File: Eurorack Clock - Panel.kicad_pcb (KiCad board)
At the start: 2 copper layers, 30 x 128.5 mm, 18 parts, among them J10X CLK/16, J3X Clock In, J6X CLK, J7X CLK/2, J8X CLK/4, J9X CLK/8, SW1X RotaryEncoder_DualWithSwitch, SW2X Run/Stop, SW3X Reset

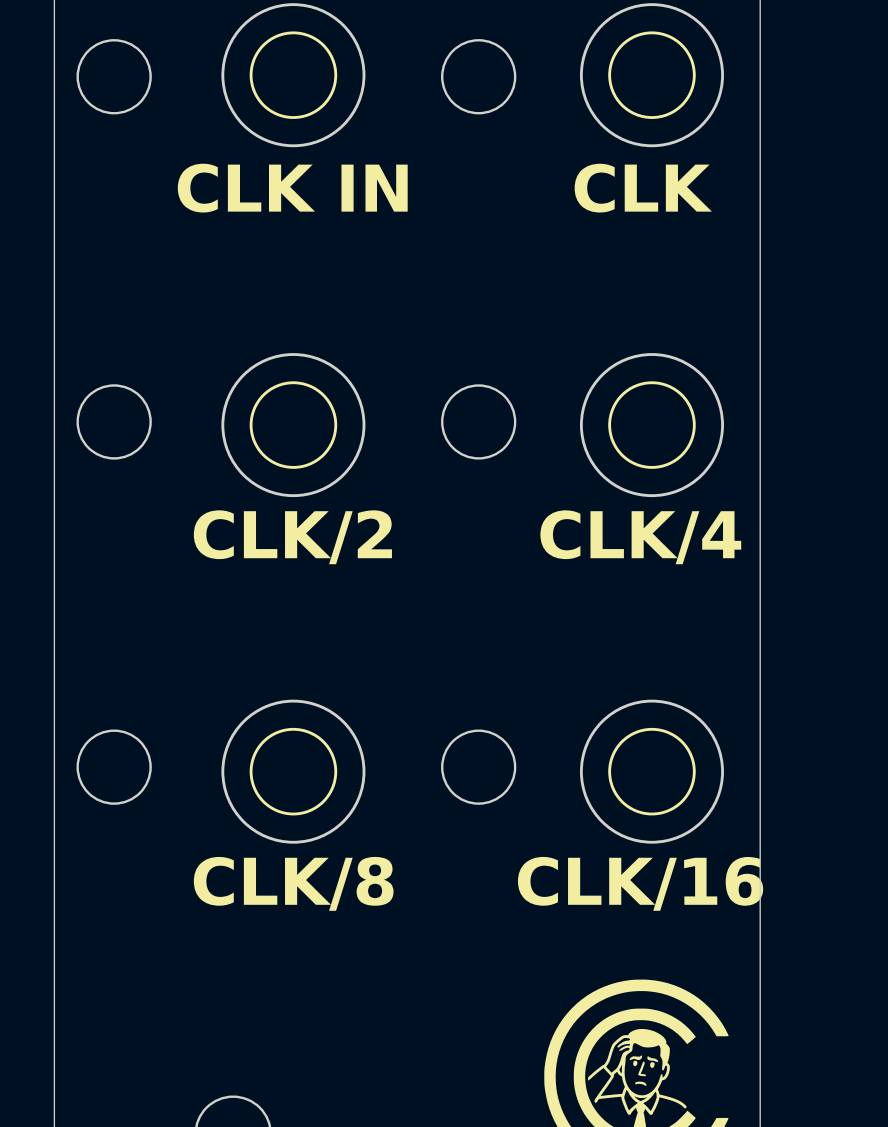
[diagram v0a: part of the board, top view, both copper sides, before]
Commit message: Updated labels on front panel
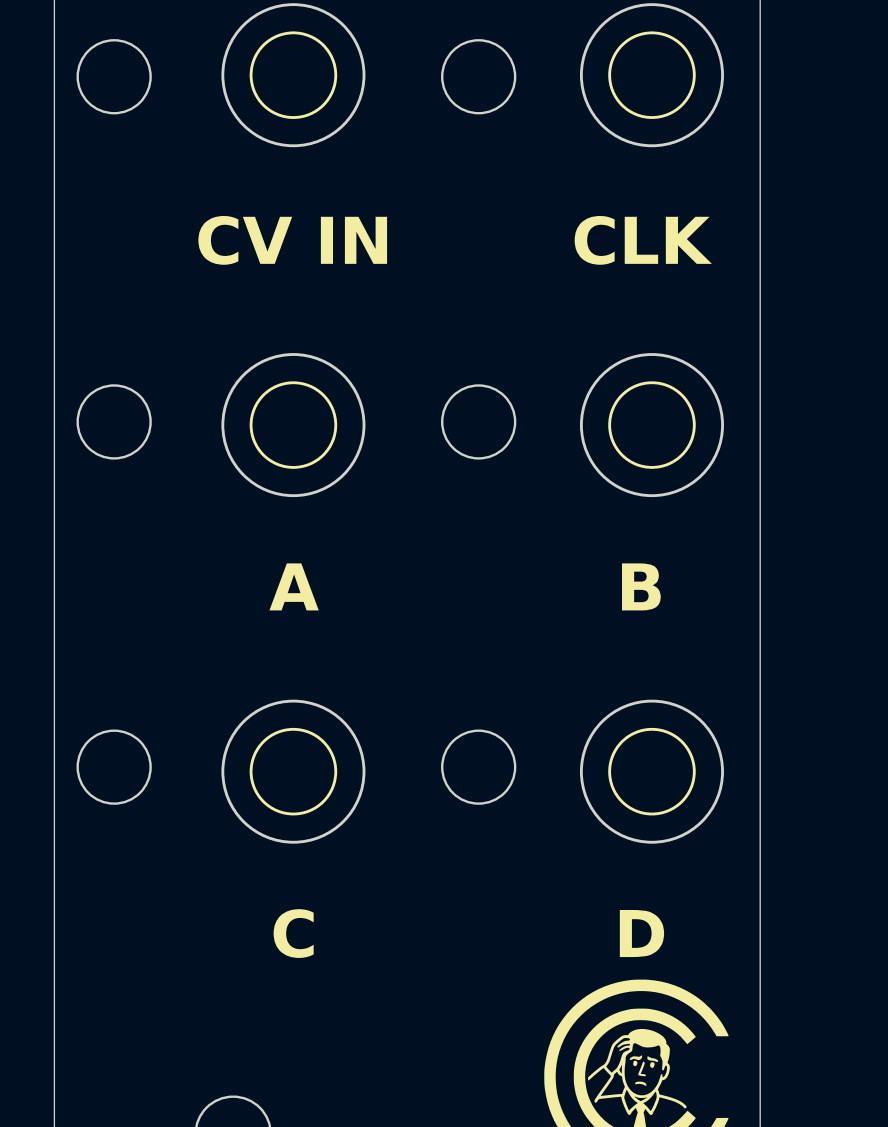
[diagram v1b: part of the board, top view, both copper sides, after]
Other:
- board text added: "A"
- board text added: "B"
- board text added: "C"
- board text added: "CV IN"
- board text added: "D"
- board text removed: "CLK IN"
- board text removed: "CLK/16"
- board text removed: "CLK/2"
- board text removed: "CLK/4"
- board text removed: "CLK/8"
